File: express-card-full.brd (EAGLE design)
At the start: 30 x 65 mm, 1 part

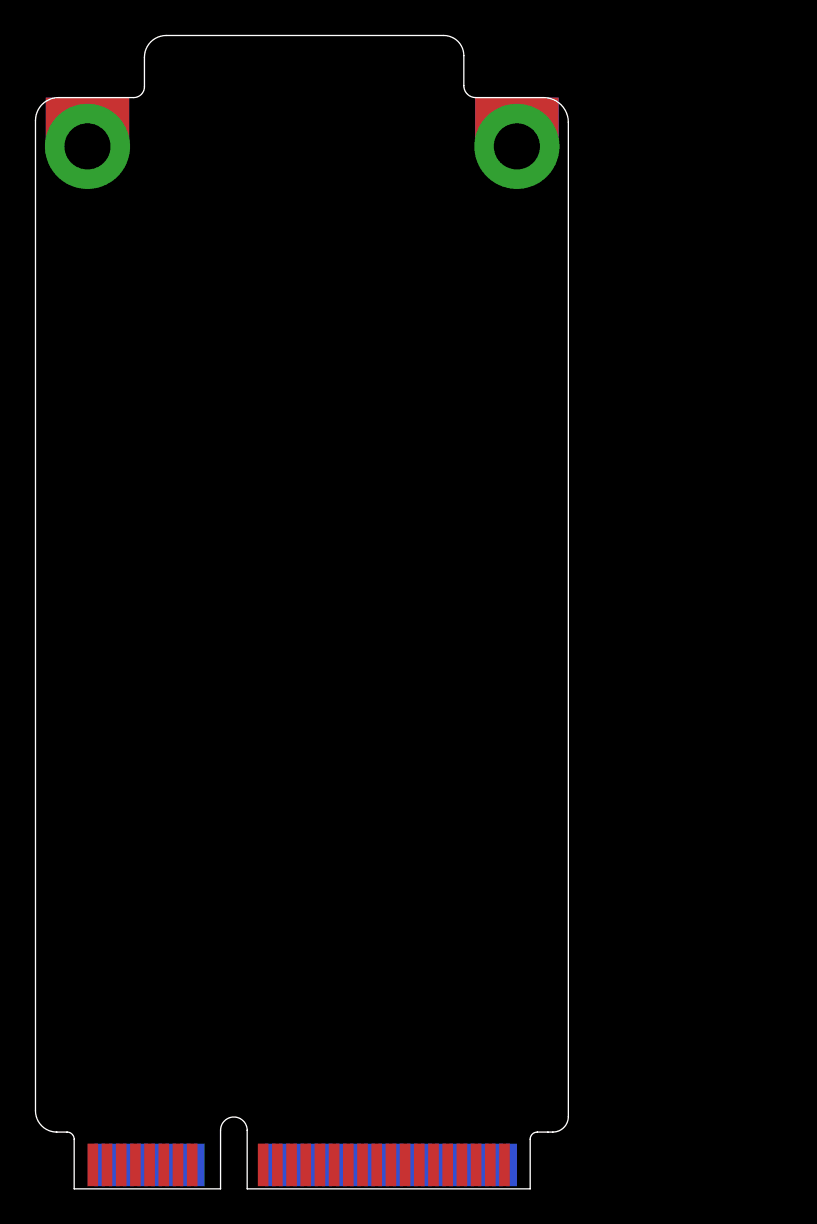
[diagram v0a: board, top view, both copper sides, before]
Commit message: board placement into positive values
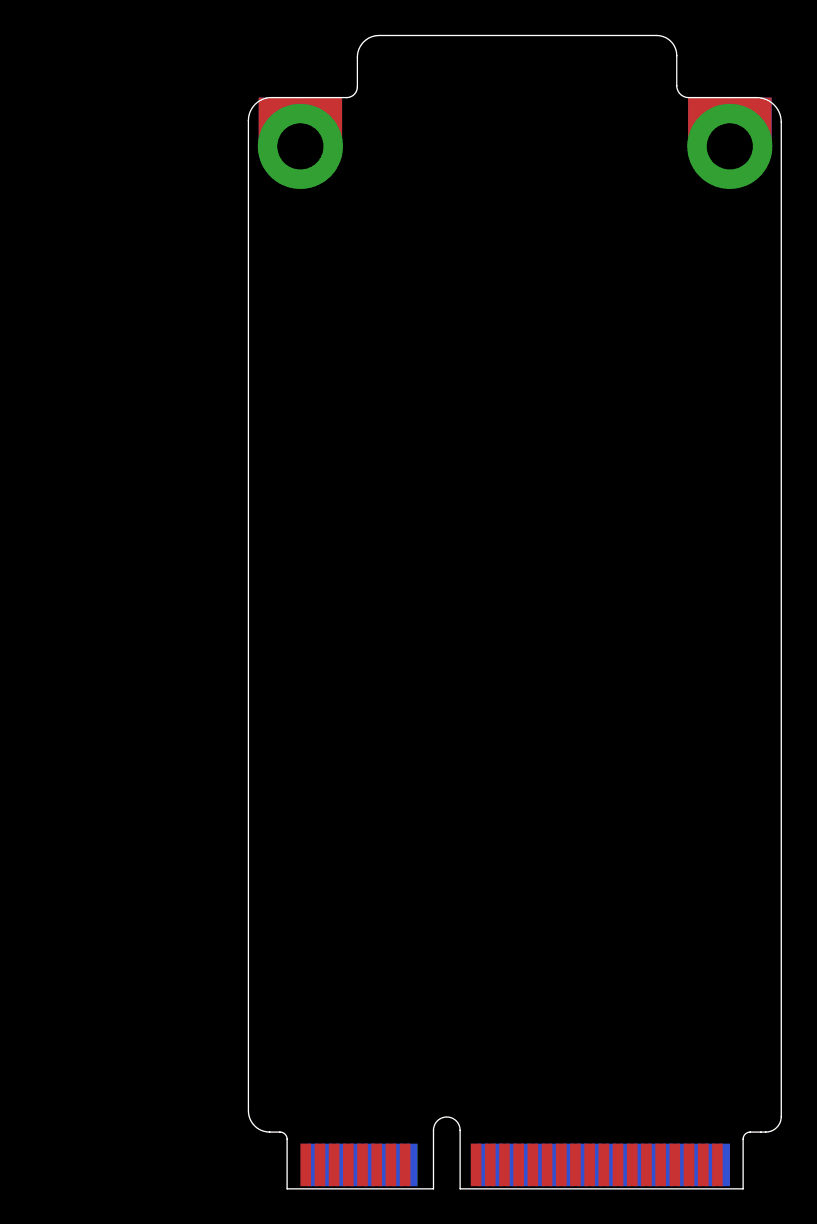
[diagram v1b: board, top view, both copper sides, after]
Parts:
- moved U$1 12.0 mm to (12.0, 0.00)
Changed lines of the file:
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@@
 <setting verticaltext="up"/>
 </settings>
-<grid distance="0.01" unitdist="mm" unit="mm" style="lines" multiple="1" display="yes" altdistance="0.025" altunitdist="inch" altunit="inch"/>
+<grid distance="1" unitdist="mm" unit="mm" style="lines" multiple="1" display="yes" altdistance="0.025" altunitdist="inch" altunit="inch"/>
 <layers>
 <layer number="1" name="Top" color="4" fill="1" visible="yes" active="yes"/>
@@
 <board>
 <plain>
-<wire x1="-0.75" y1="0.1" x2="-0.75" y2="3.4" width="0" layer="20"/>
-<wire x1="0.75" y1="0.1" x2="0.75" y2="3.4" width="0" layer="20"/>
-<wire x1="-0.75" y1="3.4" x2="0.75" y2="3.4" width="0" layer="20" curve="-180"/>
-<wire x1="-0.75" y1="0.1" x2="-9" y2="0.1" width="0" layer="20"/>
-<wire x1="-9" y1="0.1" x2="-9" y2="2.9" width="0" layer="20"/>
-<wire x1="-9.4" y1="3.3" x2="-9.983171875" y2="3.3" width="0" layer="20"/>
-<wire x1="-9.983171875" y1="3.3" x2="-11.18" y2="4.496828125" width="0" layer="20" curve="-90"/>
-<wire x1="-11.18" y1="4.496828125" x2="-11.18" y2="60.3067875" width="0" layer="20"/>
-<wire x1="-11.18" y1="60.3067875" x2="-9.8867875" y2="61.6" width="0" layer="20" curve="-90"/>
-<wire x1="-9.8867875" y1="61.6" x2="-5.6495875" y2="61.6" width="0" layer="20"/>
-<wire x1="-9.4" y1="3.3" x2="-9" y2="2.9" width="0" layer="20" curve="-90"/>
-<wire x1="18.85" y1="60.20985625" x2="18.85" y2="4.173209375" width="0" layer="20"/>
-<wire x1="18.85" y1="4.173209375" x2="17.976790625" y2="3.3" width="0" layer="20" curve="-90"/>
-<wire x1="17.976790625" y1="3.3" x2="17.7" y2="3.3" width="0" layer="20"/>
-<wire x1="0.75" y1="0.1" x2="16.7" y2="0.1" width="0" layer="20"/>
-<wire x1="16.7" y1="0.1" x2="16.7" y2="2.9" width="0" layer="20"/>
-<wire x1="17.7" y1="3.3" x2="17.1" y2="3.3" width="0" layer="20"/>
-<wire x1="17.1" y1="3.3" x2="16.7" y2="2.9" width="0" layer="20" curve="90"/>
-<wire x1="-5.6495875" y1="61.6" x2="-5.04" y2="62.2095875" width="0" layer="20" curve="90"/>
-<wire x1="-5.04" y1="62.2095875" x2="-5.04" y2="63.874603125" width="0" layer="20"/>
-<wire x1="18.85" y1="60.20985625" x2="17.45985625" y2="61.6" width="0" layer="20" curve="90"/>
-<wire x1="12.96" y1="63.967925" x2="12.96" y2="62.272009375" width="0" layer="20"/>
-<wire x1="12.96" y1="62.272009375" x2="13.632009375" y2="61.6" width="0" layer="20" curve="90"/>
-<wire x1="13.632009375" y1="61.6" x2="17.45985625" y2="61.6" width="0" layer="20"/>
-<wire x1="-5.04" y1="63.874603125" x2="-3.814603125" y2="65.1" width="0" layer="20" curve="-90"/>
-<wire x1="-3.814603125" y1="65.1" x2="11.827925" y2="65.1" width="0" layer="20"/>
-<wire x1="11.827925" y1="65.1" x2="12.96" y2="63.967925" width="0" layer="20" curve="-90"/>
+<wire x1="11.25" y1="0.1" x2="11.25" y2="3.4" width="0" layer="20"/>
+<wire x1="12.75" y1="0.1" x2="12.75" y2="3.4" width="0" layer="20"/>
+<wire x1="11.25" y1="3.4" x2="12.75" y2="3.4" width="0" layer="20" curve="-180"/>
+<wire x1="11.25" y1="0.1" x2="3" y2="0.1" width="0" layer="20"/>
+<wire x1="3" y1="0.1" x2="3" y2="2.9" width="0" layer="20"/>
+<wire x1="2.6" y1="3.3" x2="2.016828125" y2="3.3" width="0" layer="20"/>
+<wire x1="2.016828125" y1="3.3" x2="0.82" y2="4.496828125" width="0" layer="20" curve="-90"/>
+<wire x1="0.82" y1="4.496828125" x2="0.82" y2="60.3067875" width="0" layer="20"/>
+<wire x1="0.82" y1="60.3067875" x2="2.1132125" y2="61.6" width="0" layer="20" curve="-90"/>
+<wire x1="2.1132125" y1="61.6" x2="6.3504125" y2="61.6" width="0" layer="20"/>
+<wire x1="2.6" y1="3.3" x2="3" y2="2.9" width="0" layer="20" curve="-90"/>
+<wire x1="30.85" y1="60.20985625" x2="30.85" y2="4.173209375" width="0" layer="20"/>
+<wire x1="30.85" y1="4.173209375" x2="29.976790625" y2="3.3" width="0" layer="20" curve="-90"/>
+<wire x1="29.976790625" y1="3.3" x2="29.7" y2="3.3" width="0" layer="20"/>
+<wire x1="12.75" y1="0.1" x2="28.7" y2="0.1" width="0" layer="20"/>
+<wire x1="28.7" y1="0.1" x2="28.7" y2="2.9" width="0" layer="20"/>
+<wire x1="29.7" y1="3.3" x2="29.1" y2="3.3" width="0" layer="20"/>
+<wire x1="29.1" y1="3.3" x2="28.7" y2="2.9" width="0" layer="20" curve="90"/>
+<wire x1="6.3504125" y1="61.6" x2="6.96" y2="62.2095875" width="0" layer="20" curve="90"/>
+<wire x1="6.96" y1="62.2095875" x2="6.96" y2="63.874603125" width="0" layer="20"/>
+<wire x1="30.85" y1="60.20985625" x2="29.45985625" y2="61.6" width="0" layer="20" curve="90"/>
+<wire x1="24.96" y1="63.967925" x2="24.96" y2="62.272009375" width="0" layer="20"/>
+<wire x1="24.96" y1="62.272009375" x2="25.632009375" y2="61.6" width="0" layer="20" curve="90"/>
+<wire x1="25.632009375" y1="61.6" x2="29.45985625" y2="61.6" width="0" layer="20"/>
+<wire x1="6.96" y1="63.874603125" x2="8.185396875" y2="65.1" width="0" layer="20" curve="-90"/>
+<wire x1="8.185396875" y1="65.1" x2="23.827925" y2="65.1" width="0" layer="20"/>
+<wire x1="23.827925" y1="65.1" x2="24.96" y2="63.967925" width="0" layer="20" curve="-90"/>
 </plain>
 <attributes>
@@
 </autorouter>
 <elements>
-<element name="U$1" library="teensy-express" package="FULL-MINI-PCI-E" value="FULL-MINI-PCI-E" x="0" y="0"/>
+<element name="U$1" library="teensy-express" package="FULL-MINI-PCI-E" value="FULL-MINI-PCI-E" x="12" y="0"/>
 </elements>
 <signals>
@@
 <contactref element="U$1" pad="LATCH@1"/>
 <contactref element="U$1" pad="LATCH@2"/>
-<wire x1="-8.25" y1="58.85" x2="15.95" y2="58.85" width="0" layer="19" extent="1-1"/>
+<wire x1="3.75" y1="58.85" x2="27.95" y2="58.85" width="0" layer="19" extent="1-1"/>
 </signal>
 </signals>
